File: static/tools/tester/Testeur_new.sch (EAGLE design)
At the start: 33 parts, among them IC1 MEGA8-P, Q2 MFR475V

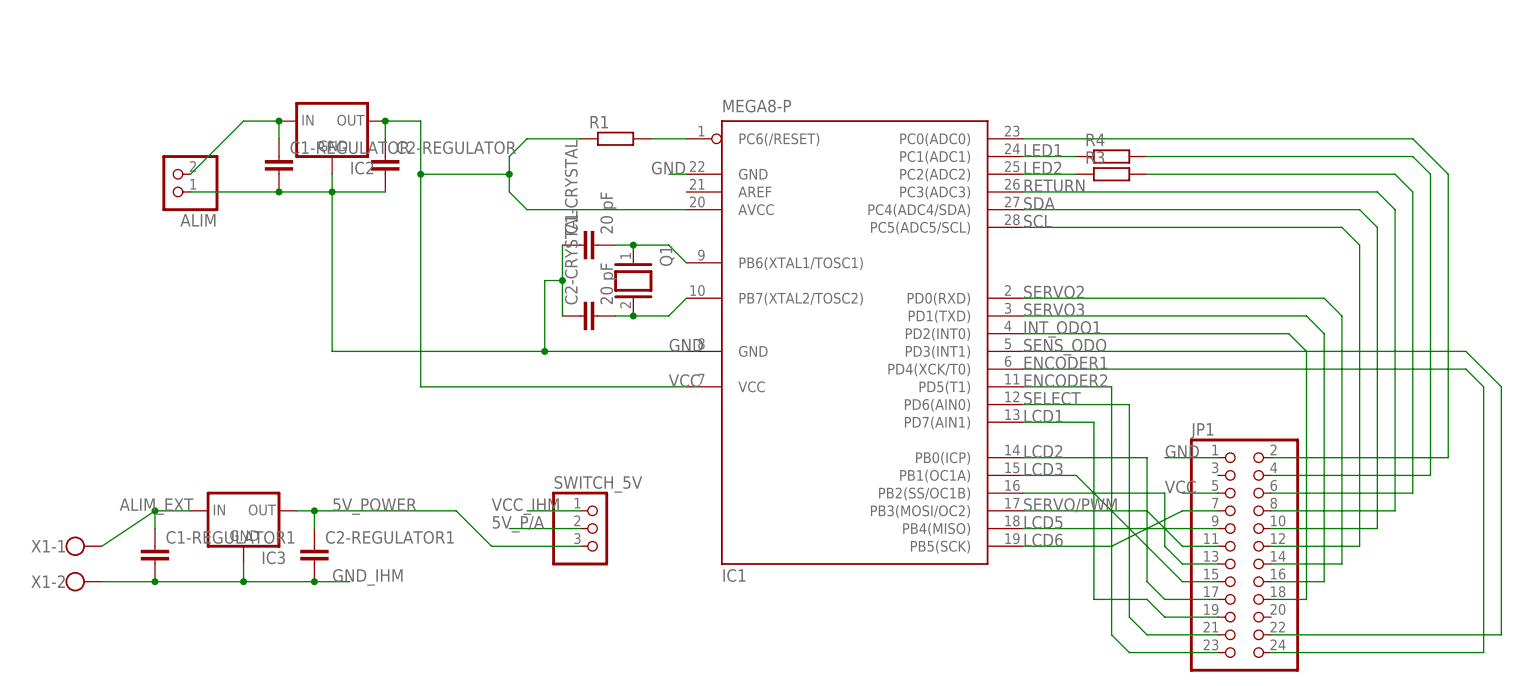
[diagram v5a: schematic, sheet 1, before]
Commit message: [tester] add "pont diviseur" and some modification.
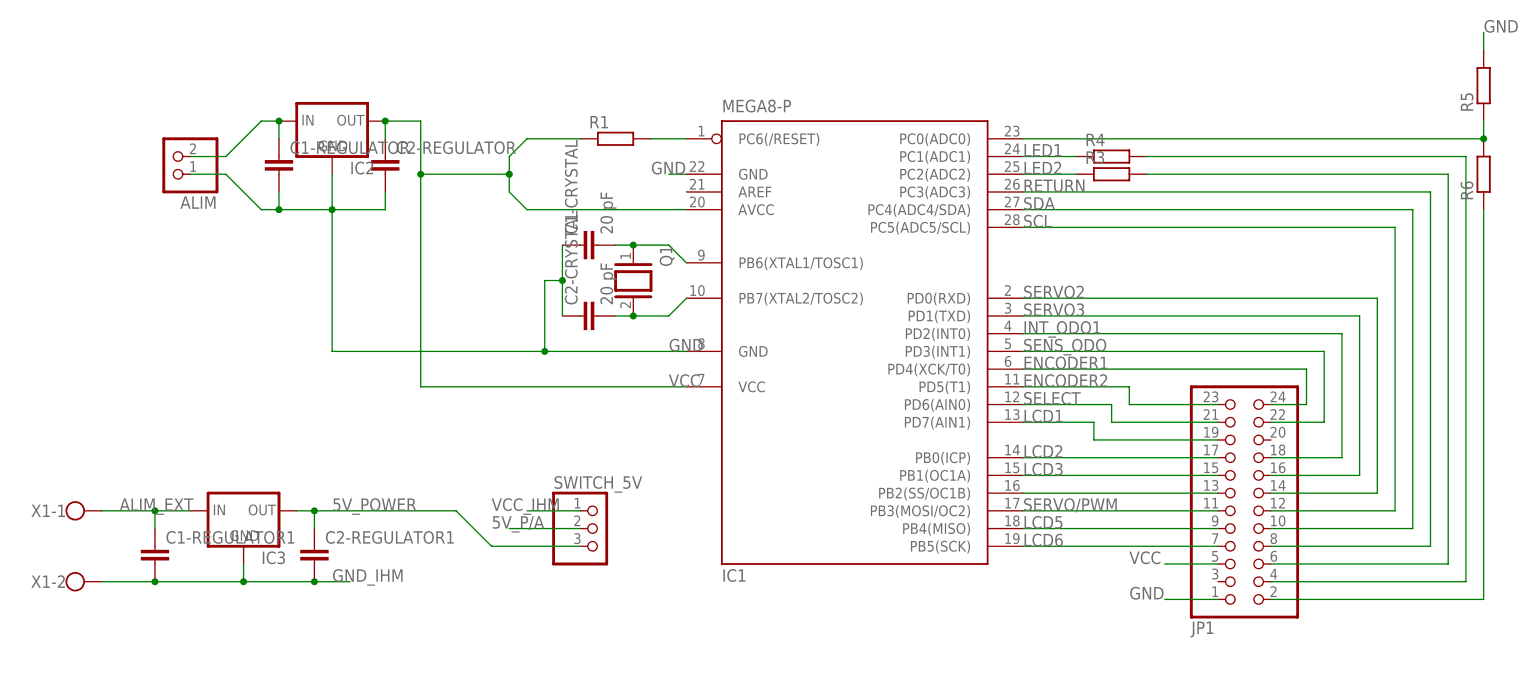
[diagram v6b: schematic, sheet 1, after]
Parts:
- added R5, R6: (no value), rcl:R-EU_0204/7
- R3, R4: device resistor:R-EU_0204/5 -> resistor:R-EU_0204/7
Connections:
- new net N$46: IC1.PC0(ADC0), R5.1, R6.2
- net GND: now also R5.2
- net N$3: now also R6.1; no longer IC1.PC0(ADC0)
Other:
- moved on the sheet: ALIM, JP1, X1-1

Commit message: [Tester] new design.
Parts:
- removed ALIM: (no value), pinhead:PINHD-1X2
- removed C1-CRYSTAL, C2-CRYSTAL: 20 pF, capacitor-wima:C5/5
- removed C1-REGULATOR, C1-REGULATOR1, C2-REGULATOR, C2-REGULATOR1: (no value), capacitor-wima:C5/5
- removed ENCODER-IHM: CI-11, piher:CI-11
- removed IC2, IC3: (no value), v-reg:78XXS
- removed JP1, JP2: (no value), pinhead:PINHD-2X12
- removed JP3: (no value), pinhead:PINHD-1X16
- removed Q1: (no value), special:XTAL/S
- removed R6: (no value), rcl:R-EU_0204/7
- removed SERVO-IHM, SERVO-IHM1, SERVO-IHM2: (no value), con-lstb:MA03-1
- removed SWITCH_5V: (no value), pinhead:PINHD-1X3
- removed X1: (no value), con-wago-500:W237-102
- added 0->3, 10->13, A0->A3: (no value), pinhead:PINHD-1X4
- added C1, C2: (no value), capacitor-wima:C5/3.5
- added ENCODER: CI-11, piher:CI-11
- added I²C: (no value), pinhead:PINHD-1X2
- added LCD: (no value), pinhead:PINHD-1X16
- added LCD_WIRES: (no value), pinhead:PINHD-1X6
- added PWM, SWITCH, SWITCH1: (no value), pinhead:PINHD-1X3
- added SERVO1, SERVO2: (no value), con-lstb:MA03-1
- added X2: (no value), con-wago-500:W237-102
- IC1: value MEGA8-P -> (none); device atmel:MEGA8-P -> v-reg:78XXS
- R3, R4: device resistor:R-EU_0204/7 -> rcl:R-EU_0204/7
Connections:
- removed net 5V_P/A: SERVO-IHM.2, SERVO-IHM1.2, SERVO-IHM2.2, SWITCH_5V.2
- removed net 5V_POW_IHM: JP2.3
- removed net ENCODER1: IC1.PD4(XCK/T0), JP1.24
- removed net ENCODER2: IC1.PD5(T1), JP1.23
- removed net GND_IHM: AR.1, C1-REGULATOR1.2, C2-REGULATOR1.2, CODER-IHM.2, ENCODER-IHMA.B, ENCODER-IHMB.D, I2C-IHM.2, IC3.GND, JP2.1, JP3.1, JP3.10, JP3.5, JP3.7, JP3.8, JP3.9, LED1.C, LED2.C, POTAR.3, Q2.E, RETURN_IHM.1, SERVO-IHM.1, SERVO-IHM1.1, SERVO-IHM2.1, X1-2.KL
- removed net INT_ODO1: IC1.PD2(INT0), JP1.18
- removed net LCD1: IC1.PD7(AIN1), JP1.19
- removed net LCD2: IC1.PB0(ICP), JP1.17
- removed net LCD3: IC1.PB1(OC1A), JP1.15
- removed net LCD5: IC1.PB4(MISO), JP1.9
- removed net LCD6: IC1.PB5(SCK), JP1.7
- removed net LED1: IC1.PC1(ADC1), R4.1
- removed net LED2: IC1.PC2(ADC2), R3.1
- removed net N$27: JP2.15, JP3.11
- removed net N$28: JP1.4, R4.2
- removed net N$29: JP2.13, JP3.12
- removed net N$30: JP2.9, JP3.13
- removed net N$34: JP2.7, JP3.14
- removed net N$35: JP2.11, R2.1, SERVO-IHM.3
- removed net N$36: JP2.8, RETURN_IHM.2
- removed net N$46: IC1.PC0(ADC0), R5.1, R6.2
- removed net N$7: JP1.6, R3.2
- removed net RETURN: IC1.PC3(ADC3), JP1.8
- removed net SCL: IC1.PC5(ADC5/SCL), JP1.12
- removed net SDA: IC1.PC4(ADC4/SDA), JP1.10
- removed net SELECT: IC1.PD6(AIN0), JP1.21
- removed net SENS_ODO: IC1.PD3(INT1), JP1.22
- removed net SERVO/PWM: IC1.PB3(MOSI/OC2), JP1.11
- removed net SERVO2: IC1.PD0(RXD), JP1.14
- removed net SERVO3: IC1.PD1(TXD), JP1.16
- removed net VCC: C2-REGULATOR.1, IC1.AVCC, IC1.VCC@1, IC2.OUT, JP1.5, R1.1
- removed net VCC_IHM: CODER-IHM.1, I2C-IHM.1, JP2.5, JP3.2, POTAR.2, SWITCH_5V.1
- new net 5V_ARDUINO: CODER-IHM.1, I2C-IHM.1, LCD.2, POTAR.2, SWITCH.3
- new net 5V_EXT: C2.1, IC1.OUT, SWITCH.1
- new net N$15: 10->13.3, PWM.3, R2.1
- new net N$24: AR.2, R4.2
- new net N$5: A0->A3.2, ENCODERA.C
- new net POWER: PWM.2, SERVO1.2, SERVO2.2, SWITCH1.2
- net 5V_POWER: now also SWITCH.2, SWITCH1.1; no longer C2-REGULATOR1.1, IC3.OUT, SWITCH_5V.3
- net ALIM_EXT: now also C1.1, IC1.IN, SWITCH1.3, X2-1.KL; no longer C1-REGULATOR1.1, IC3.IN, X1-1.KL
- net GND: now also AR.1, C1.2, C2.2, CODER-IHM.2, ENCODERA.B, ENCODERB.D, I2C-IHM.2, LCD.1, LCD.10, LCD.5, LCD.7, LCD.8, LCD.9, LED1.C, LED2.C, POTAR.3, PWM.1, Q2.E, R5.1, RETURN_IHM.1, SERVO1.1, SERVO2.1, X2-2.KL; no longer ALIM.1, C1-CRYSTAL.1, C1-REGULATOR.2, C2-CRYSTAL.1, C2-REGULATOR.2, IC1.GND@1, IC2.GND, JP1.1, R5.2
- net N$1: now also A0->A3.3, RETURN_IHM.2; no longer C1-CRYSTAL.2, IC1.PB6(XTAL1/TOSC1), Q1.1
- net N$10: now also I²C.2; no longer JP2.10
- net N$11: now also I²C.1; no longer JP2.12
- net N$12: now also R1.2; no longer JP2.4
- net N$13: now also 10->13.4, ENCODERB.E; no longer JP2.6, LED2.A
- net N$14: now also 0->3.4, SERVO1.3; no longer JP2.14, SERVO-IHM1.3
- net N$16: now also 0->3.2; no longer JP2.18
- net N$17: now also 0->3.1; no longer JP2.22
- net N$18: now also A0->A3.1, ENCODERA.A; no longer ENCODER-IHMA.A, JP2.24
- net N$2: now also LCD.11, LCD_WIRES.4; no longer C2-CRYSTAL.2, IC1.PB7(XTAL2/TOSC2), Q1.2
- net N$21: now also 10->13.2, R1.1; no longer ENCODER-IHMA.C, JP2.23
- net N$22: now also 10->13.1, R3.1; no longer ENCODER-IHMB.E, JP2.21
- net N$25: now also LCD.4, LCD_WIRES.6; no longer JP2.19, JP3.4
- net N$26: now also LCD.6, LCD_WIRES.5; no longer JP2.17, JP3.6
- net N$3: now also LCD.12, LCD_WIRES.3; no longer JP1.2, R6.1
- net N$37: now also A0->A3.4, R4.1, R5.2; no longer AR.2, JP2.2
- net N$39: now also LCD.3; no longer JP3.3
- net N$4: now also LCD.13, LCD_WIRES.2; no longer IC1.PC6(/RESET), R1.2
- net N$42: now also 0->3.3, SERVO2.3; no longer JP2.16, SERVO-IHM2.3
- net N$6: now also LCD.14, LCD_WIRES.1; no longer ALIM.2, C1-REGULATOR.1, IC2.IN
- net N$9: now also LED2.A, R3.2; no longer IC1.PB2(SS/OC1B), JP1.13

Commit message: [tester] continue new design.
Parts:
- added TO_ARD: (no value), pinhead:PINHD-1X2
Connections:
- net 5V_ARDUINO: now also TO_ARD.1
- net GND: now also TO_ARD.2
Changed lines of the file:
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@@
 <part name="R5" library="rcl" deviceset="R-EU_" device="0204/7"/>
 <part name="SWITCH1" library="pinhead" deviceset="PINHD-1X3" device=""/>
+<part name="TO_ARD" library="pinhead" deviceset="PINHD-1X2" device=""/>
 </parts>
 <sheets>
@@
 <instance part="R5" gate="G$1" x="88.9" y="86.36" rot="R90"/>
 <instance part="SWITCH1" gate="A" x="-30.48" y="-22.86"/>
+<instance part="TO_ARD" gate="G$1" x="0" y="63.5"/>
 </instances>
 <busses>
@@
 <label x="88.9" y="78.74" size="1.778" layer="95"/>
 </segment>
+<segment>
+<pinref part="TO_ARD" gate="G$1" pin="2"/>
+<wire x1="-2.54" y1="63.5" x2="-7.62" y2="63.5" width="0.1524" layer="91"/>
+<wire x1="-7.62" y1="63.5" x2="-7.62" y2="60.96" width="0.1524" layer="91"/>
+<wire x1="-7.62" y1="60.96" x2="-20.32" y2="60.96" width="0.1524" layer="91"/>
+<label x="-20.32" y="60.96" size="1.778" layer="95"/>
+</segment>
 </net>
 <net name="N$10" class="0">
@@
 <label x="88.9" y="53.34" size="1.778" layer="95"/>
 </segment>
-</net>
+<segment>
+<pinref part="TO_ARD" gate="G$1" pin="1"/>
+<wire x1="-2.54" y1="66.04" x2="-20.32" y2="66.04" width="0.1524" layer="91"/>
+<label x="-22.86" y="66.04" size="1.778" layer="95"/>
+</segment>
+</net>
